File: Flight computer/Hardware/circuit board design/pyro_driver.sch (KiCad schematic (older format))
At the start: 19 parts, among them J4 Conn_01x06_Female, U5 Si7232DN, U6 Si7232DN

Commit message: removed the 37khz crystal
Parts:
- removed J4: Conn_01x06_Female, TerminalBlock_TE-Connectivity:TerminalBlock_TE_282834-6_1x06_P2.54mm_Horizontal, symbol Connector:Conn_01x06_Female
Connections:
- wire segments 68 -> 60
- no-connect marks 2 -> 0
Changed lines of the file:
@@
 $Descr A4 11693 8268
 encoding utf-8
-Sheet 4 7
+Sheet 5 7
 Title "Pyro drivers"
 Date "2019-09-02"
@@
 Put in a block connector, like the TE connectivity ones\n
 $Comp
-L Connector:Conn_01x06_Female J4
-U 1 1 5D6BBFA3
-P 2100 4100
-F 0 "J4" H 2128 4076 50  0000 L CNN
-F 1 "Conn_01x06_Female" H 2128 3985 50  0000 L CNN
-F 2 "TerminalBlock_TE-Connectivity:TerminalBlock_TE_282834-6_1x06_P2.54mm_Horizontal" H 2100 4100 50  0001 C CNN
-F 3 "~" H 2100 4100 50  0001 C CNN
-	1    2100 4100
-	1    0    0    -1
-$EndComp
-NoConn ~ 1900 4300
-NoConn ~ 1900 4400
-Text Label 1350 3900 2    50   ~ 0
-FET_A
-Wire Wire Line
-	1350 3900 1900 3900
-$Comp
 L circuit-board-design-rescue:Si7232DN-Driver_FET U?
 U 2 1 5D743B81
@@
 Text Label 7450 2750 0    50   ~ 0
 FET_B
-Text Label 1350 4100 2    50   ~ 0
-FET_B
-Wire Wire Line
-	1350 4100 1900 4100
 Wire Wire Line
 	5850 3500 5850 3250
-$Comp
-L power:GND #PWR045
-U 1 1 5D70E267
-P 1600 4900
-F 0 "#PWR045" H 1600 4650 50  0001 C CNN
-F 1 "GND" H 1605 4727 50  0000 C CNN
-F 2 "" H 1600 4900 50  0001 C CNN
-F 3 "" H 1600 4900 50  0001 C CNN
-	1    1600 4900
-	1    0    0    -1
-$EndComp
-Wire Wire Line
-	1900 4000 1600 4000
-Wire Wire Line
-	1600 4000 1600 4700
-Wire Wire Line
-	1900 4200 1700 4200
-Wire Wire Line
-	1700 4700 1600 4700
-Wire Wire Line
-	1700 4200 1700 4700
-Connection ~ 1600 4700
-Wire Wire Line
-	1600 4700 1600 4900
 Wire Wire Line
 	4950 1800 5550 1800

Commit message: fixed errors with symbol and footprint connections
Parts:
- U5, U6: symbol circuit-board-design-rescue:Si7232DN-Driver_FET -> flight-computer:Si7232DN
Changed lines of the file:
@@
 $EndDescr
 $Comp
-L circuit-board-design-rescue:Si7232DN-Driver_FET U6
+L flight-computer:Si7232DN U6
 U 1 1 5D696EFB
 P 5850 1350
@@
 Put in a block connector, like the TE connectivity ones\n
 $Comp
-L circuit-board-design-rescue:Si7232DN-Driver_FET U?
+L flight-computer:Si7232DN U?
 U 2 1 5D743B81
 P 5850 2600
@@
 	4950 3050 5550 3050
 $Comp
-L circuit-board-design-rescue:Si7232DN-Driver_FET U?
+L flight-computer:Si7232DN U?
 U 1 1 5D7DA597
 P 5850 4000
@@
 FIRE_C
 $Comp
-L circuit-board-design-rescue:Si7232DN-Driver_FET U?
+L flight-computer:Si7232DN U?
 U 2 1 5D7DA5FD
 P 5850 5250

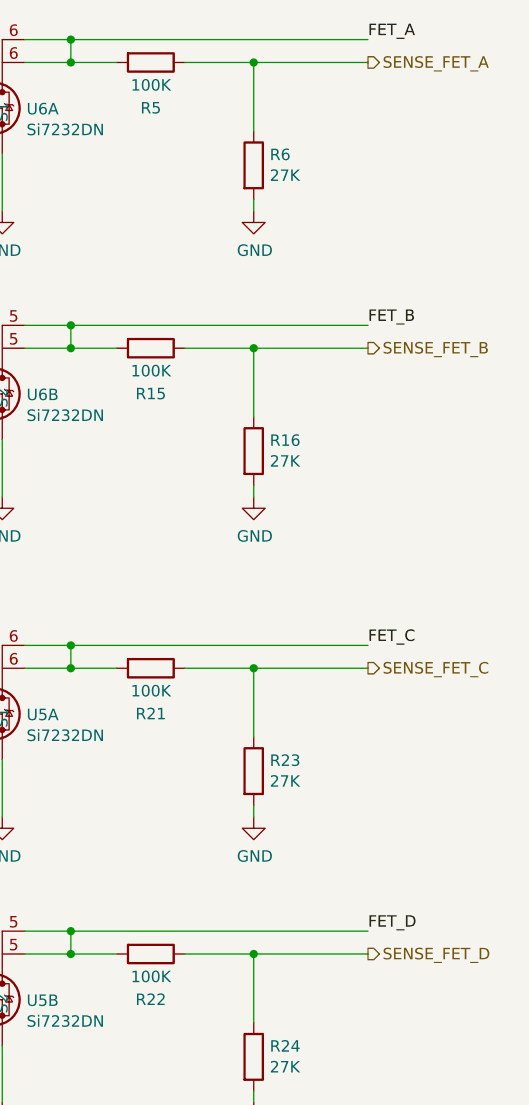
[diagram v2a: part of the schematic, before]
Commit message: added in LDO based power supply
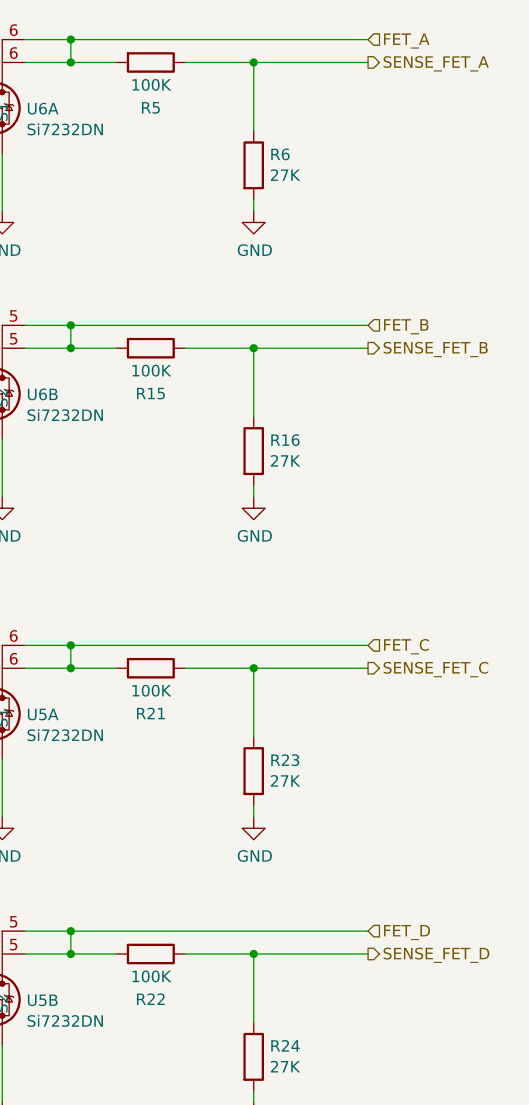
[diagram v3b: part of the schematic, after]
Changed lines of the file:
@@
 Text HLabel 7450 1600 2    50   Output ~ 0
 SENSE_FET_A
-Text Label 7450 1500 0    50   ~ 0
-FET_A
 Wire Wire Line
 	4450 1800 4450 1950
@@
 Text HLabel 7450 2850 2    50   Output ~ 0
 SENSE_FET_B
-Text Label 7450 2750 0    50   ~ 0
-FET_B
 Wire Wire Line
 	5850 3500 5850 3250
@@
 Text HLabel 7450 4250 2    50   Output ~ 0
 SENSE_FET_C
-Text Label 7450 4150 0    50   ~ 0
-FET_C
 Wire Wire Line
 	4450 4450 4450 4600
@@
 Text HLabel 7450 5500 2    50   Output ~ 0
 SENSE_FET_D
-Text Label 7450 5400 0    50   ~ 0
-FET_D
 Wire Wire Line
 	5850 6150 5850 5900
@@
 Wire Wire Line
 	4950 5700 5550 5700
+Text HLabel 7450 1500 2    50   Input ~ 0
+FET_A
+Text HLabel 7450 2750 2    50   Input ~ 0
+FET_B
+Text HLabel 7450 4150 2    50   Input ~ 0
+FET_C
+Text HLabel 7450 5400 2    50   Input ~ 0
+FET_D
 $EndSCHEMATC

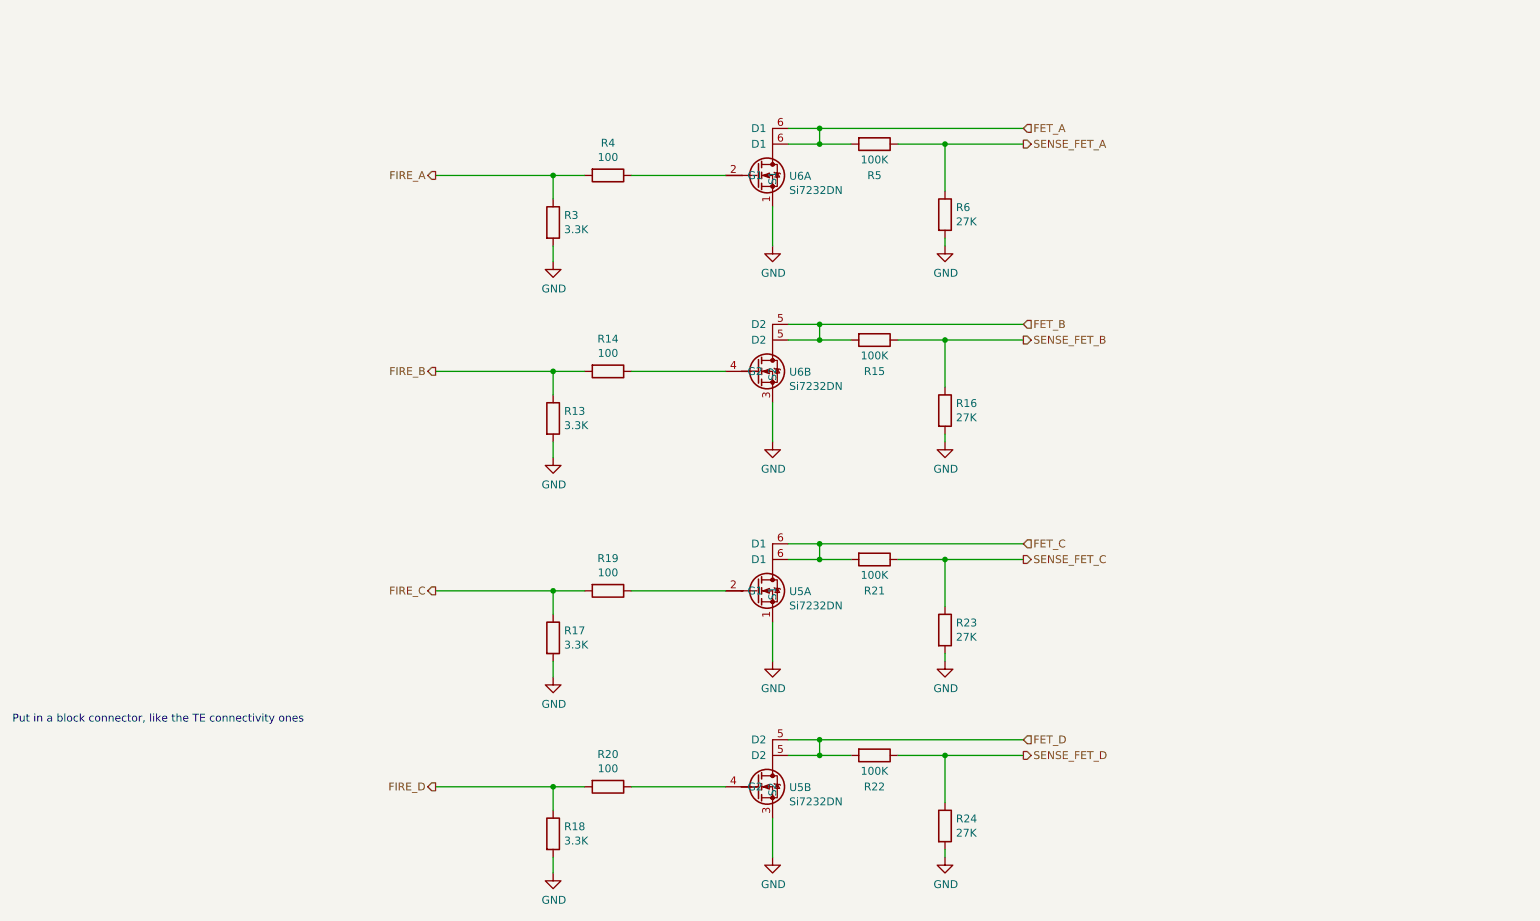
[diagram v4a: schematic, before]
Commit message: set up the PCB to fit formfactor
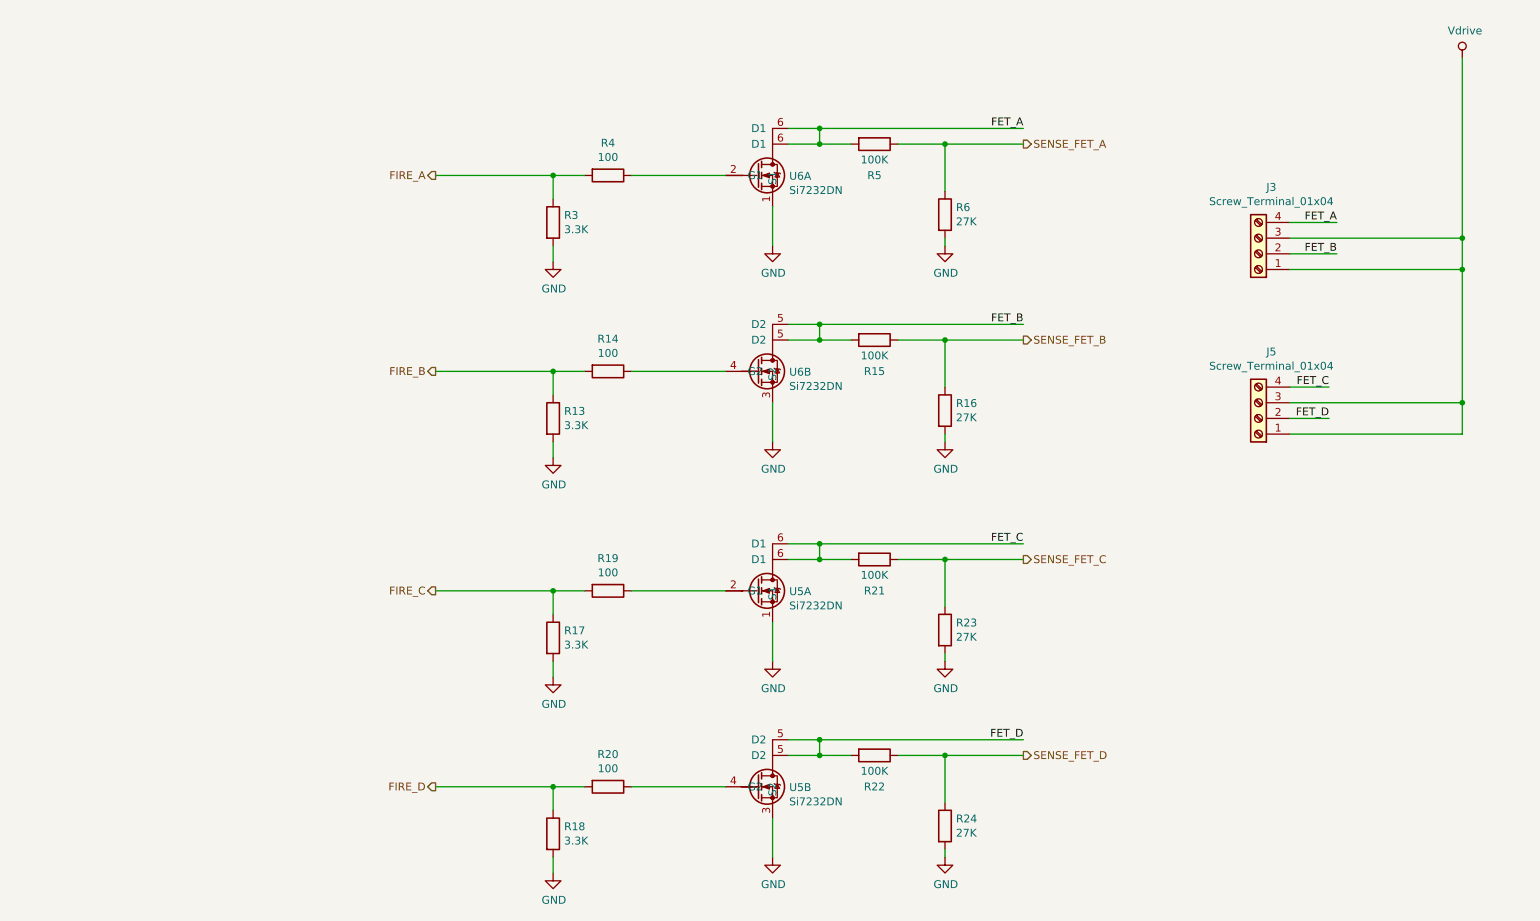
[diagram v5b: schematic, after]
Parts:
- added J3, J5: Screw_Terminal_01x04, TerminalBlock_TE-Connectivity:TerminalBlock_TE_282834-4_1x04_P2.54mm_Horizontal, symbol Connector:Screw_Terminal_01x04
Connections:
- net FET_A: now also J3.4 (Pin_4)
- net FET_B: now also J3.2 (Pin_2)
- net FET_C: now also J5.4 (Pin_4)
- net FET_D: now also J5.2 (Pin_2)
- new net Vdrive: J3.1 (Pin_1), J3.3 (Pin_3), J5.1 (Pin_1), J5.3 (Pin_3)
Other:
- note removed: "Put in a block connector, like the TE connectivity ones\n"
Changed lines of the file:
@@
 Text HLabel 3700 1800 0    50   Output ~ 0
 FIRE_A
-Text Notes 1000 5300 0    50   ~ 0
-Put in a block connector, like the TE connectivity ones\n
 $Comp
 L flight-computer:Si7232DN U?
@@
 Wire Wire Line
 	4950 5700 5550 5700
-Text HLabel 7450 1500 2    50   Input ~ 0
+$Comp
+L Connector:Screw_Terminal_01x04 J?
+U 1 1 5D7D6AC3
+P 8950 2300
+AR Path="/5D5B1705/5D7D6AC3" Ref="J?"  Part="1"
+AR Path="/5D6468D5/5D7D6AC3" Ref="J3"  Part="1"
+F 0 "J3" H 8868 1875 50  0000 C CNN
+F 1 "Screw_Terminal_01x04" H 8868 1966 50  0000 C CNN
+F 2 "TerminalBlock_TE-Connectivity:TerminalBlock_TE_282834-4_1x04_P2.54mm_Horizontal" H 8950 2300 50  0001 C CNN
+F 3 "~" H 8950 2300 50  0001 C CNN
+	1    8950 2300
+	-1   0    0    1
+$EndComp
+$Comp
+L Connector:Screw_Terminal_01x04 J?
+U 1 1 5D7D6AC9
+P 8950 3350
+AR Path="/5D5B1705/5D7D6AC9" Ref="J?"  Part="1"
+AR Path="/5D6468D5/5D7D6AC9" Ref="J5"  Part="1"
+F 0 "J5" H 8868 2925 50  0000 C CNN
+F 1 "Screw_Terminal_01x04" H 8868 3016 50  0000 C CNN
+F 2 "TerminalBlock_TE-Connectivity:TerminalBlock_TE_282834-4_1x04_P2.54mm_Horizontal" H 8950 3350 50  0001 C CNN
+F 3 "~" H 8950 3350 50  0001 C CNN
+	1    8950 3350
+	-1   0    0    1
+$EndComp
+Text Label 7450 1500 2    50   ~ 0
 FET_A
-Text HLabel 7450 2750 2    50   Input ~ 0
+Text Label 7450 2750 2    50   ~ 0
 FET_B
-Text HLabel 7450 4150 2    50   Input ~ 0
+Text Label 7450 4150 2    50   ~ 0
 FET_C
-Text HLabel 7450 5400 2    50   Input ~ 0
+Text Label 7450 5400 2    50   ~ 0
 FET_D
+Wire Wire Line
+	9150 2200 10250 2200
+Wire Wire Line
+	10250 2200 10250 1050
+Wire Wire Line
+	9150 2400 10250 2400
+Wire Wire Line
+	10250 2400 10250 2200
+Connection ~ 10250 2200
+Connection ~ 10250 2400
+Wire Wire Line
+	9150 3250 10250 3250
+Wire Wire Line
+	10250 2400 10250 3250
+Wire Wire Line
+	9150 3450 10250 3450
+Wire Wire Line
+	10250 3450 10250 3250
+Connection ~ 10250 3250
+$Comp
+L power:Vdrive #PWR0112
+U 1 1 5D7E2F36
+P 10250 1050
+F 0 "#PWR0112" H 10050 900 50  0001 C CNN
+F 1 "Vdrive" H 10267 1223 50  0000 C CNN
+F 2 "" H 10250 1050 50  0001 C CNN
+F 3 "" H 10250 1050 50  0001 C CNN
+	1    10250 1050
+	1    0    0    -1
+$EndComp
+Text Label 9450 2100 2    50   ~ 0
+FET_A
+Wire Wire Line
+	9450 2100 9150 2100
+Text Label 9450 2300 2    50   ~ 0
+FET_B
+Wire Wire Line
+	9150 2300 9450 2300
+Text Label 9400 3150 2    50   ~ 0
+FET_C
+Wire Wire Line
+	9400 3150 9150 3150
+Text Label 9400 3350 2    50   ~ 0
+FET_D
+Wire Wire Line
+	9400 3350 9150 3350
 $EndSCHEMATC

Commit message: removed the 100 ohm resistors on the gate of the pyro mosfets
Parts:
- removed R14, R19, R20, R4: 100, Resistor_SMD:R_0603_1608Metric, symbol Device:R
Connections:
- net FIRE_A: now also U6.2 (G1)
- net FIRE_B: now also U6.4 (G2)
- net FIRE_C: now also U5.2 (G1)
- net FIRE_D: now also U5.4 (G2)
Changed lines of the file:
@@
 Wire Wire Line
 	4450 2250 4450 2350
-$Comp
-L Device:R R4
-U 1 1 5D6B06F6
-P 4800 1800
-F 0 "R4" V 4593 1800 50  0000 C CNN
-F 1 "100" V 4684 1800 50  0000 C CNN
-F 2 "Resistor_SMD:R_0603_1608Metric" V 4730 1800 50  0001 C CNN
-F 3 "~" H 4800 1800 50  0001 C CNN
-	1    4800 1800
-	0    1    1    0
-$EndComp
-Wire Wire Line
-	4650 1800 4450 1800
 Text HLabel 3700 1800 0    50   Output ~ 0
 FIRE_A
@@
 	5850 3500 5850 3250
 Wire Wire Line
-	4950 1800 5550 1800
-Wire Wire Line
 	4450 3050 4450 3200
 Connection ~ 4450 3050
@@
 Wire Wire Line
 	4450 3500 4450 3600
-$Comp
-L Device:R R14
-U 1 1 5D743BDF
-P 4800 3050
-F 0 "R14" V 4593 3050 50  0000 C CNN
-F 1 "100" V 4684 3050 50  0000 C CNN
-F 2 "Resistor_SMD:R_0603_1608Metric" V 4730 3050 50  0001 C CNN
-F 3 "~" H 4800 3050 50  0001 C CNN
-	1    4800 3050
-	0    1    1    0
-$EndComp
-Wire Wire Line
-	4650 3050 4450 3050
 Text HLabel 3700 3050 0    50   Output ~ 0
 FIRE_B
-Wire Wire Line
-	4950 3050 5550 3050
 $Comp
 L flight-computer:Si7232DN U?
@@
 Wire Wire Line
 	4450 4900 4450 5000
-$Comp
-L Device:R R19
-U 1 1 5D7DA5F0
-P 4800 4450
-F 0 "R19" V 4593 4450 50  0000 C CNN
-F 1 "100" V 4684 4450 50  0000 C CNN
-F 2 "Resistor_SMD:R_0603_1608Metric" V 4730 4450 50  0001 C CNN
-F 3 "~" H 4800 4450 50  0001 C CNN
-	1    4800 4450
-	0    1    1    0
-$EndComp
-Wire Wire Line
-	4650 4450 4450 4450
 Text HLabel 3700 4450 0    50   Output ~ 0
 FIRE_C
@@
 	5850 6150 5850 5900
 Wire Wire Line
-	4950 4450 5550 4450
-Wire Wire Line
 	4450 5700 4450 5850
 Connection ~ 4450 5700
@@
 Wire Wire Line
 	4450 6150 4450 6250
-$Comp
-L Device:R R20
-U 1 1 5D7DA657
-P 4800 5700
-F 0 "R20" V 4593 5700 50  0000 C CNN
-F 1 "100" V 4684 5700 50  0000 C CNN
-F 2 "Resistor_SMD:R_0603_1608Metric" V 4730 5700 50  0001 C CNN
-F 3 "~" H 4800 5700 50  0001 C CNN
-	1    4800 5700
-	0    1    1    0
-$EndComp
-Wire Wire Line
-	4650 5700 4450 5700
 Text HLabel 3700 5700 0    50   Output ~ 0
 FIRE_D
-Wire Wire Line
-	4950 5700 5550 5700
 $Comp
 L Connector:Screw_Terminal_01x04 J?
@@
 Wire Wire Line
 	9400 3350 9150 3350
+Wire Wire Line
+	4450 1800 5550 1800
+Wire Wire Line
+	4450 3050 5550 3050
+Wire Wire Line
+	4450 4450 5550 4450
+Wire Wire Line
+	4450 5700 5550 5700
 $EndSCHEMATC
